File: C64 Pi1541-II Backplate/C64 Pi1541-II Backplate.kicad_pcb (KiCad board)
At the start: 2 copper layers, 97.8 x 97.8 mm, 5 parts, among them M1 Mounting, M2 Mounting, M3 Mounting, M4 Mounting

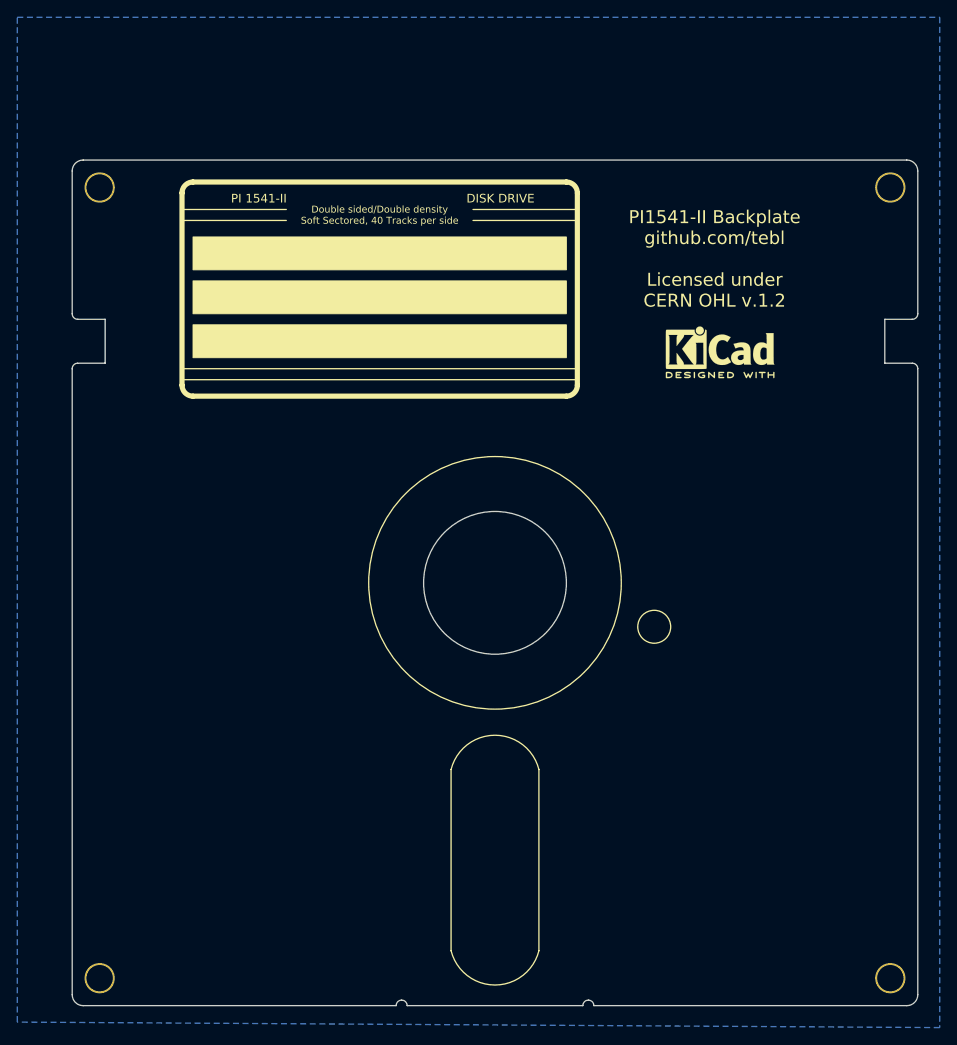
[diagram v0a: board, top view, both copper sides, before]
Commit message: Added copper layer to backplate
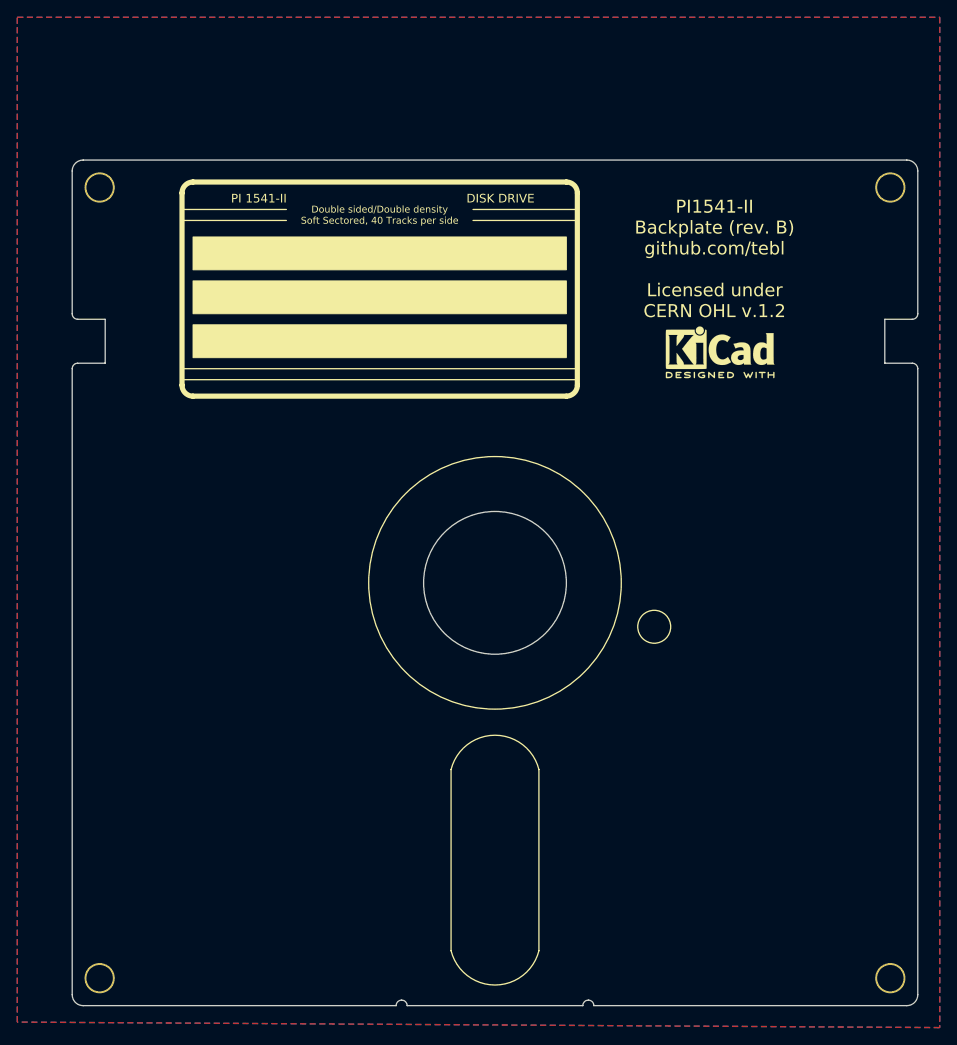
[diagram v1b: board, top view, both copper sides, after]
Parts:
- M1, M2, M3, M4: footprint mounting:M3 -> mounting:M3_pin
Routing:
- added copper zone on B.Cu, net Net-(M1-Pad1)
- added copper zone on F.Cu, net Net-(M1-Pad1)
- removed copper zone on B.Cu, net GND
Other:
- board text added: "PI1541-II Backplate (rev. B) github.com/tebl Licensed under CERN OHL v.1.2"
- board text removed: "PI1541-II Backplate github.com/tebl Licensed under CERN OHL v.1.2"
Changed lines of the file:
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@@
   (page A4)
   (layers
-    (0 F.Cu signal)
-    (31 B.Cu signal)
+    (0 F.Cu signal hide)
+    (31 B.Cu signal hide)
     (32 B.Adhes user)
     (33 F.Adhes user)
@@
   )
   (net 0 "")
-  (net 1 GND)
+  (net 1 "Net-(M1-Pad1)")
   (net_class Default "This is the default net class."
     (clearance 0.2)
@@
     (uvia_dia 0.3)
     (uvia_drill 0.1)
+    (add_net "Net-(M1-Pad1)")
   )
   (net_class Power ""
@@
     (uvia_dia 0.3)
     (uvia_drill 0.1)
-  )
-  (module mounting:M3 (layer F.Cu)
-    (at 75.565 149.225)
-    (descr "module 1 pin (ou trou mecanique de percage)")
-    (tags DEV)
-    (fp_text reference M1 (at 0 -3.048) (layer F.Fab) hide
-      (effects (font (size 1 1) (thickness 0.15)))
-    )
-    (fp_text value Mounting (at 0 3) (layer F.Fab) hide
-      (effects (font (size 1 1) (thickness 0.15)))
-    )
-    (fp_circle (center 0 0) (end 2.6 0) (layer F.CrtYd) (width 0.05))
-    (fp_circle (center 0 0) (end 2 0.8) (layer F.Fab) (width 0.1))
-    (pad "" np_thru_hole circle (at 0 0) (size 3.5 3.5) (drill 3.048) (layers *.Cu *.Mask)
-      (solder_mask_margin 0.8))
-  )
-  (module mounting:M3 (layer F.Cu)
-    (at 167.005 149.225)
-    (descr "module 1 pin (ou trou mecanique de percage)")
-    (tags DEV)
-    (fp_text reference M2 (at 0 -3.048) (layer F.Fab) hide
-      (effects (font (size 1 1) (thickness 0.15)))
-    )
-    (fp_text value Mounting (at 0 3) (layer F.Fab) hide
-      (effects (font (size 1 1) (thickness 0.15)))
-    )
-    (fp_circle (center 0 0) (end 2.6 0) (layer F.CrtYd) (width 0.05))
-    (fp_circle (center 0 0) (end 2 0.8) (layer F.Fab) (width 0.1))
-    (pad "" np_thru_hole circle (at 0 0) (size 3.5 3.5) (drill 3.048) (layers *.Cu *.Mask)
-      (solder_mask_margin 0.8))
-  )
-  (module mounting:M3 (layer F.Cu)
-    (at 167.005 57.785)
-    (descr "module 1 pin (ou trou mecanique de percage)")
-    (tags DEV)
-    (fp_text reference M3 (at 0 -3.048) (layer F.Fab) hide
-      (effects (font (size 1 1) (thickness 0.15)))
-    )
-    (fp_text value Mounting (at 0 3) (layer F.Fab) hide
-      (effects (font (size 1 1) (thickness 0.15)))
-    )
-    (fp_circle (center 0 0) (end 2.6 0) (layer F.CrtYd) (width 0.05))
-    (fp_circle (center 0 0) (end 2 0.8) (layer F.Fab) (width 0.1))
-    (pad "" np_thru_hole circle (at 0 0) (size 3.5 3.5) (drill 3.048) (layers *.Cu *.Mask)
-      (solder_mask_margin 0.8))
-  )
-  (module mounting:M3 (layer F.Cu)
-    (at 75.565 57.785)
-    (descr "module 1 pin (ou trou mecanique de percage)")
-    (tags DEV)
-    (fp_text reference M4 (at 0 -3.048) (layer F.Fab) hide
-      (effects (font (size 1 1) (thickness 0.15)))
-    )
-    (fp_text value Mounting (at 0 3) (layer F.Fab) hide
-      (effects (font (size 1 1) (thickness 0.15)))
-    )
-    (fp_circle (center 0 0) (end 2.6 0) (layer F.CrtYd) (width 0.05))
-    (fp_circle (center 0 0) (end 2 0.8) (layer F.Fab) (width 0.1))
-    (pad "" np_thru_hole circle (at 0 0) (size 3.5 3.5) (drill 3.048) (layers *.Cu *.Mask)
-      (solder_mask_margin 0.8))
   )
   (module Symbols:KiCad-Logo2_6mm_SilkScreen locked (layer F.Cu)
@@
       (xy -6.229974 2.276739) (xy -6.202883 2.270457) (xy -6.167082 2.268653) (xy -6.121371 2.269066)) (layer F.SilkS) (width 0.01))
   )
+  (module mounting:M3_pin (layer F.Cu)
+    (at 75.565 149.225)
+    (descr "module 1 pin (ou trou mecanique de percage)")
+    (tags DEV)
+    (fp_text reference M1 (at 0 -3.048) (layer F.Fab) hide
+      (effects (font (size 1 1) (thickness 0.15)))
+    )
+    (fp_text value Mounting (at 0 3) (layer F.Fab) hide
+      (effects (font (size 1 1) (thickness 0.15)))
+    )
+    (fp_circle (center 0 0) (end 2.6 0) (layer F.CrtYd) (width 0.05))
+    (fp_circle (center 0 0) (end 2 0.8) (layer F.Fab) (width 0.1))
+    (pad 1 thru_hole circle (at 0 0) (size 3.5 3.5) (drill 3.048) (layers *.Cu *.Mask)
+      (net 1 "Net-(M1-Pad1)") (solder_mask_margin 0.8))
+  )
+  (module mounting:M3_pin (layer F.Cu)
+    (at 167.005 149.225)
+    (descr "module 1 pin (ou trou mecanique de percage)")
+    (tags DEV)
+    (fp_text reference M2 (at 0 -3.048) (layer F.Fab) hide
+      (effects (font (size 1 1) (thickness 0.15)))
+    )
+    (fp_text value Mounting (at 0 3) (layer F.Fab) hide
+      (effects (font (size 1 1) (thickness 0.15)))
+    )
+    (fp_circle (center 0 0) (end 2 0.8) (layer F.Fab) (width 0.1))
+    (fp_circle (center 0 0) (end 2.6 0) (layer F.CrtYd) (width 0.05))
+    (pad 1 thru_hole circle (at 0 0) (size 3.5 3.5) (drill 3.048) (layers *.Cu *.Mask)
+      (net 1 "Net-(M1-Pad1)") (solder_mask_margin 0.8))
+  )
+  (module mounting:M3_pin (layer F.Cu)
+    (at 167.005 57.785)
+    (descr "module 1 pin (ou trou mecanique de percage)")
+    (tags DEV)
+    (fp_text reference M3 (at 0 -3.048) (layer F.Fab) hide
+      (effects (font (size 1 1) (thickness 0.15)))
+    )
+    (fp_text value Mounting (at 0 3) (layer F.Fab) hide
+      (effects (font (size 1 1) (thickness 0.15)))
+    )
+    (fp_circle (center 0 0) (end 2.6 0) (layer F.CrtYd) (width 0.05))
+    (fp_circle (center 0 0) (end 2 0.8) (layer F.Fab) (width 0.1))
+    (pad 1 thru_hole circle (at 0 0) (size 3.5 3.5) (drill 3.048) (layers *.Cu *.Mask)
+      (net 1 "Net-(M1-Pad1)") (solder_mask_margin 0.8))
+  )
+  (module mounting:M3_pin (layer F.Cu)
+    (at 75.565 57.785)
+    (descr "module 1 pin (ou trou mecanique de percage)")
+    (tags DEV)
+    (fp_text reference M4 (at 0 -3.048) (layer F.Fab) hide
+      (effects (font (size 1 1) (thickness 0.15)))
+    )
+    (fp_text value Mounting (at 0 3) (layer F.Fab) hide
+      (effects (font (size 1 1) (thickness 0.15)))
+    )
+    (fp_circle (center 0 0) (end 2 0.8) (layer F.Fab) (width 0.1))
+    (fp_circle (center 0 0) (end 2.6 0) (layer F.CrtYd) (width 0.05))
+    (pad 1 thru_hole circle (at 0 0) (size 3.5 3.5) (drill 3.048) (layers *.Cu *.Mask)
+      (net 1 "Net-(M1-Pad1)") (solder_mask_margin 0.8))
+  )
   (gr_circle (center 121.285 103.505) (end 131.445 103.505) (layer B.Mask) (width 3.8))
   (gr_line (start 161.29 142.875) (end 170.18 151.13) (layer B.SilkS) (width 0.15))
@@
   (gr_arc (start 73.025 78.74) (end 73.025 78.105) (angle -90) (layer Edge.Cuts) (width 0.15))
   (gr_arc (start 73.025 72.39) (end 72.39 72.39) (angle -90) (layer Edge.Cuts) (width 0.15))
-  (gr_text "PI1541-II Backplate\ngithub.com/tebl\n\nLicensed under\nCERN OHL v.1.2" (at 146.685 66.04) (layer F.SilkS)
+  (gr_text "PI1541-II\nBackplate (rev. B)\ngithub.com/tebl\n\nLicensed under\nCERN OHL v.1.2" (at 146.685 66.04) (layer F.SilkS)
     (effects (font (size 1.5 1.5) (thickness 0.15)))
   )
@@
   (gr_line (start 73.66 152.4) (end 109.855 152.4) (angle 90) (layer Edge.Cuts) (width 0.15))
   (gr_arc (start 73.66 151.13) (end 73.66 152.4) (angle 90) (layer Edge.Cuts) (width 0.15))
-  (zone (net 1) (net_name GND) (layer B.Cu) (hatch edge 0.508)
+  (zone (net 1) (net_name "Net-(M1-Pad1)") (layer B.Cu) (hatch edge 0.508)
     (connect_pads (clearance 0.508))
     (min_thickness 0.254)
+    (fill yes (arc_segments 16) (thermal_gap 0.508) (thermal_bridge_width 0.508))
+    (polygon
+      (pts
+        (xy 66.04 38.1) (xy 172.72 38.1) (xy 172.72 154.94) (xy 66.04 154.305)
+      )
+    )
+  )
+  (zone (net 1) (net_name "Net-(M1-Pad1)") (layer F.Cu) (hatch edge 0.508)
+    (connect_pads (clearance 0.508))
+    (min_thickness 0.254)
